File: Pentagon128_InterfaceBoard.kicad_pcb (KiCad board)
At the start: 2 copper layers, 138.1 x 389.6 mm, 33 parts, among them J1 DIN41612_02x32_AB, J10 Tape Out, J11 Tape In, J12 Mini-DIN-6, J2 Conn_02x03_Odd_Even ATmega Pr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, J3 Conn_02x08_Odd_Even Ext Keyb, J4 Conn_02x05_Odd_Even Kempston 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, J5 DE9_Plug Kempston Out SMD, J6 DE15_Plug_HighDensity VGA CRT, J7 Conn_01x04 FDD Power, J8 Conn_01x04 Audio In, J9 AudioJack3, Q1 Q_NPN_BCE, Q2 Q_NPN_BCE, Q3 Q_NPN_BCE, Q4 Q_NPN_BCE, U1 MT8816 PLCC44, U2 ATmega168PA-A

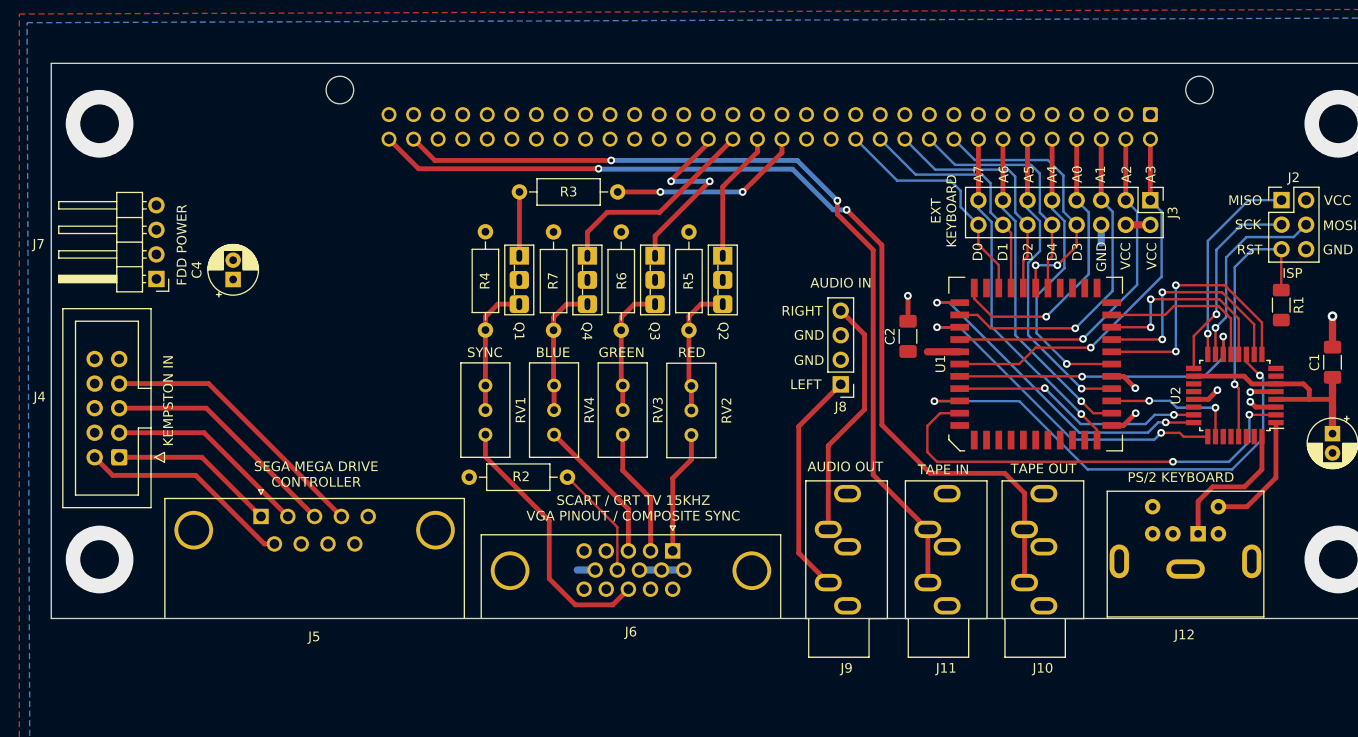
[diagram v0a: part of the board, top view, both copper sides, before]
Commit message: Add 5.5x2.1mm 5V DC external power connector.
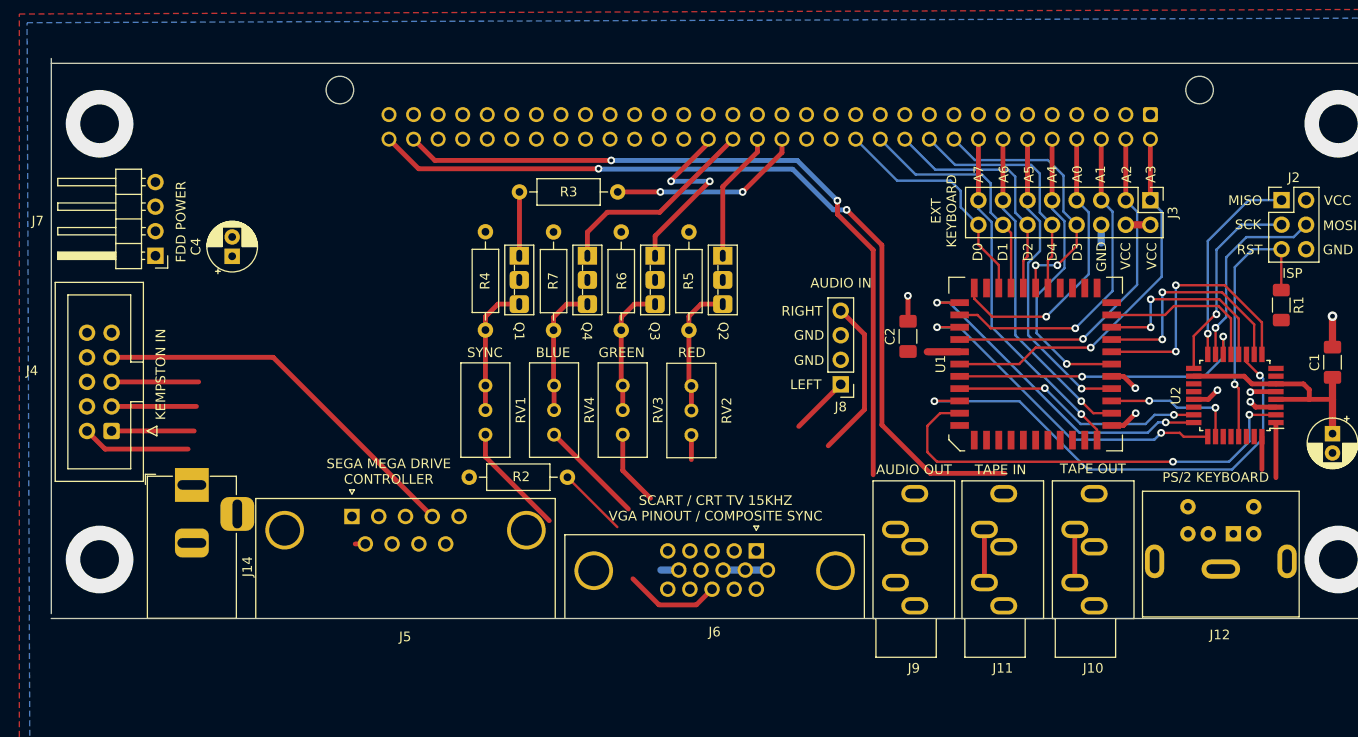
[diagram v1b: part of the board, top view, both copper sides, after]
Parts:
- added J14: Barrel_Jack_Switch, Connector_BarrelJack:BarrelJack_Horizontal, F.Cu at (69.2, 101.4)
- moved J5 9.40 mm to (85.8, 104.7)
- moved J6 8.65 mm to (127.6, 108.2)
- moved J9 6.95 mm to (144.0, 113.9)
- moved J11 5.85 mm to (153.2, 113.9)
- moved J10 5.20 mm to (162.6, 113.9)
- moved J12 3.65 mm to (176.9, 106.5)
- moved J4 2.83 mm to (60.9, 95.8)
- moved C4 2.40 mm to (73.4, 77.8)
- moved J7 2.40 mm to (65.5, 77.7)
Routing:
- net /AUDIO_LEFT: track 23.6 -> 6.14 mm
- net /LEFT: track 24.8 -> 9.00 mm
- net /DOWN: track 21.0 -> 8.78 mm
- net /DAT: track 14.7 -> 3.40 mm
- net /RIGHT: track 28.7 -> 40.0 mm
- net /CRT_RED: track 12.8 -> 2.54 mm
- net /FIRE: track 22.3 -> 12.3 mm
- net /UP: track 17.2 -> 8.55 mm
- net /AUDIO_RIGHT: track 25.2 -> 16.5 mm
- net /TAPE_IN: track 89.8 -> 81.8 mm
- net /CLK: track 12.9 -> 5.70 mm
- net /TAPE_OUT: track 101.0 -> 94.4 mm
- net /CRT_SYNC: track 27.6 -> 21.6 mm
- net /CRT_GREEN: track 13.2 -> 7.77 mm
- net Net-(J6-Pad9): track 11.8 -> 7.33 mm
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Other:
- outline, holes or cut-outs redrawn

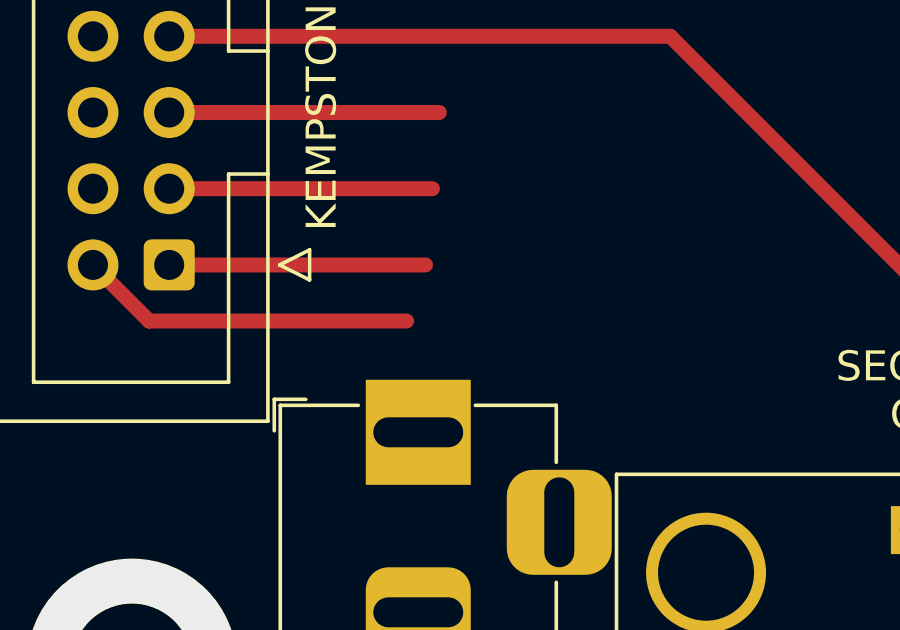
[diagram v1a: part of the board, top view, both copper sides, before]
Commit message: Add 5V DC IN markings.
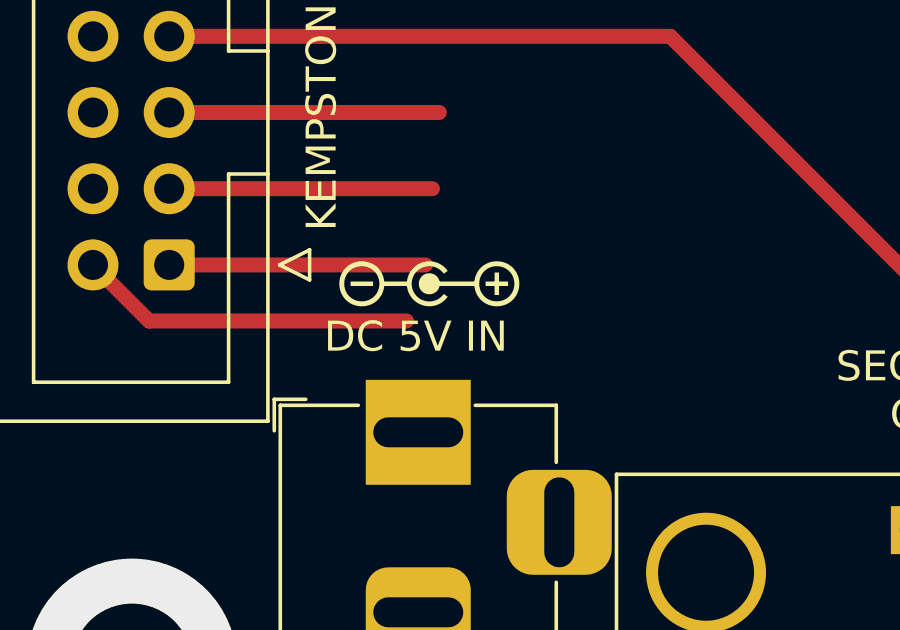
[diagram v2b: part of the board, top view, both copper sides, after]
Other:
- board text added: "DC 5V IN"

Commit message: Interface PCB dimensions based on real main PCB measurements. Replace main PCB edge from gerbers to custom placeholder. Replace vias with mounting holes, correct placement. Add mounting hole between DB9 and DB15 connectors. Move / group modules and connectors. Shorten AUDIO_IN pin markings.
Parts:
- added REF**: MountingHole_3mm, MountingHole:MountingHole_3mm, F.Cu at (197.1, 33.5)
- added REF**: MountingHole_3mm, MountingHole:MountingHole_3mm, F.Cu at (62.2, 108.2)
- added REF**: MountingHole_3mm, MountingHole:MountingHole_3mm, F.Cu at (60.7, 35.0)
- added REF**: MountingHole_3mm, MountingHole:MountingHole_3mm, F.Cu at (112.9, 108.4)
- added REF**: MountingHole_3mm, MountingHole:MountingHole_3mm, F.Cu at (197.1, 108.2)
- added REF**: MountingHole_3mm, MountingHole:MountingHole_3mm, F.Cu at (60.7, 65.8)
- added REF**: MountingHole_3mm, MountingHole:MountingHole_3mm, F.Cu at (197.1, 65.8)
- added REF**: DIN41612_Q_2x32_Female_Horizontal_THT, Connector_DIN:DIN41612_Q_2x32_Female_Horizontal_THT, F.Cu at (177.6, 35.9)
- moved RV1 21.4 mm to (121.0, 96.6)
- moved RV2 21.4 mm to (142.3, 96.6)
- moved R2 21.4 mm to (119.3, 101.0)
- moved RV3 21.4 mm to (135.2, 96.6)
- moved RV4 21.4 mm to (128.1, 96.6)
- moved Q2 19.5 mm to (143.6, 80.6)
- moved Q3 19.5 mm to (136.6, 80.6)
- moved Q4 19.5 mm to (129.6, 80.6)
- moved R5 19.5 mm to (140.1, 85.8)
- moved R6 19.5 mm to (133.1, 75.6)
- moved Q1 19.5 mm to (122.6, 80.6)
- moved R4 19.5 mm to (119.1, 85.8)
- moved R7 19.5 mm to (126.1, 75.6)
- moved R3 16.1 mm to (129.4, 71.5)
- moved J8 13.8 mm to (150.1, 91.5)
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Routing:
- net /LEFT: track 9.00 -> 37.2 mm
- net /DOWN: track 8.78 -> 33.4 mm
- net /FIRE: track 12.3 -> 34.7 mm
- net /UP: track 8.55 -> 29.6 mm
- net /AUDIO_LEFT: track 6.14 -> 22.4 mm
- net /TAPE_IN: track 81.8 -> 94.6 mm
- net /TAPE_OUT: track 94.4 -> 106.5 mm
- net /CRT_RED: track 2.54 -> 14.5 mm
- net VCC: track 31.1 -> 19.9 mm
- net /DAT: track 3.40 -> 14.5 mm
- net /AUDIO_RIGHT: track 16.5 -> 24.3 mm
- net /BLUE: track 21.5 -> 14.0 mm
- net /CLK: track 5.70 -> 12.2 mm
- net /CRT_GREEN: track 7.77 -> 12.5 mm
- net /SYNC: track 20.1 -> 15.5 mm
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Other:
- board size 138.1 x 389.6 mm -> 150 x 119 mm
- board text added: "G"
- board text added: "L"
- board text added: "R"
- board text removed: "LEFT"
- board text removed: "RIGHT"
